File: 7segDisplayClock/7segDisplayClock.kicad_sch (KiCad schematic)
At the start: 26 parts, among them J1 USB_B_Micro, Q1 NPN, Q2 NPN, Q3 NPN, Q4 NPN, SW1 SW_Push, SW2 SW_Push, U1 HDSP-7503, U2 HDSP-7503, U3 HDSP-7503, U4 HDSP-7503, U5 PIC16F506, U6 74LS48

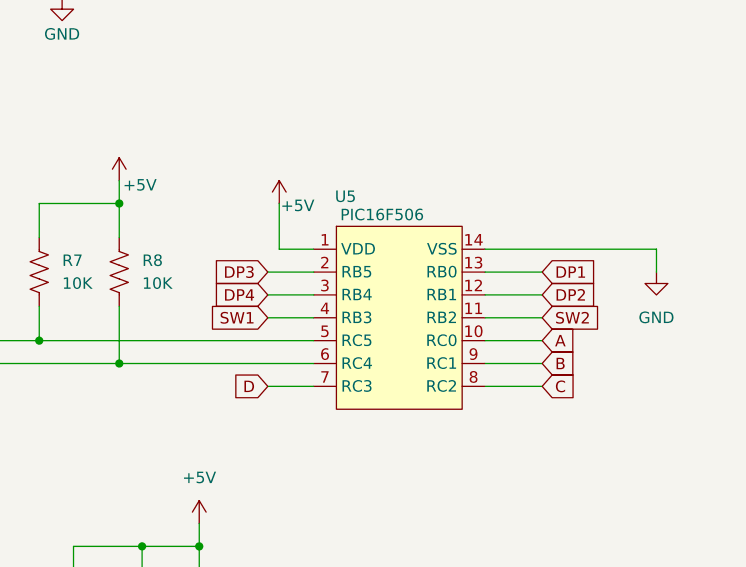
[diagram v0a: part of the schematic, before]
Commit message: BJT control signals change to match hardware
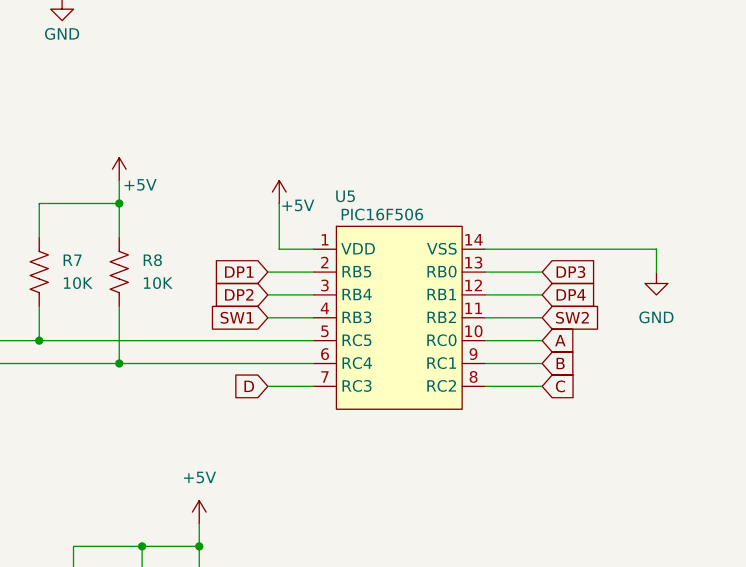
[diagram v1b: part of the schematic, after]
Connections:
- net DP1: now also U5.2 (RB5); no longer U5.13 (RB0)
- net DP2: now also U5.3 (RB4); no longer U5.12 (RB1)
- net DP3: now also U5.13 (RB0); no longer U5.2 (RB5)
- net DP4: now also U5.12 (RB1); no longer U5.3 (RB4)

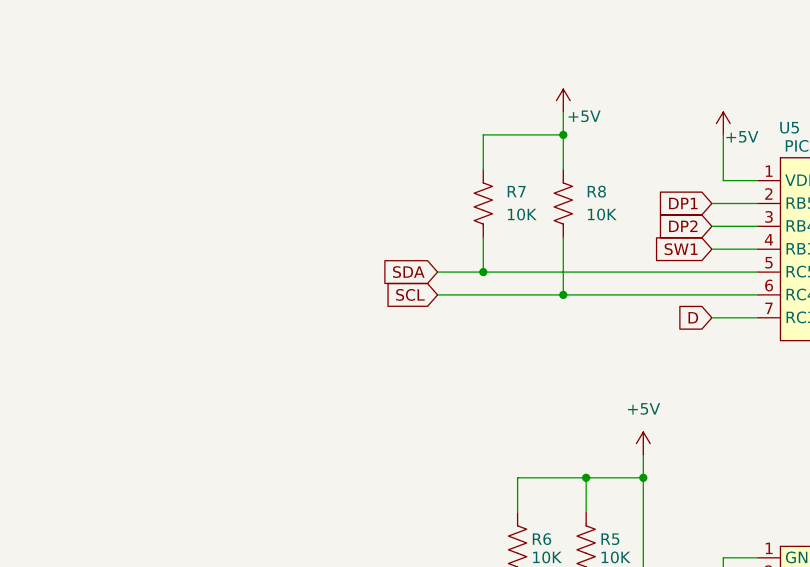
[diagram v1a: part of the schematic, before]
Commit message: SDA and SCL signals changed to match real hardware
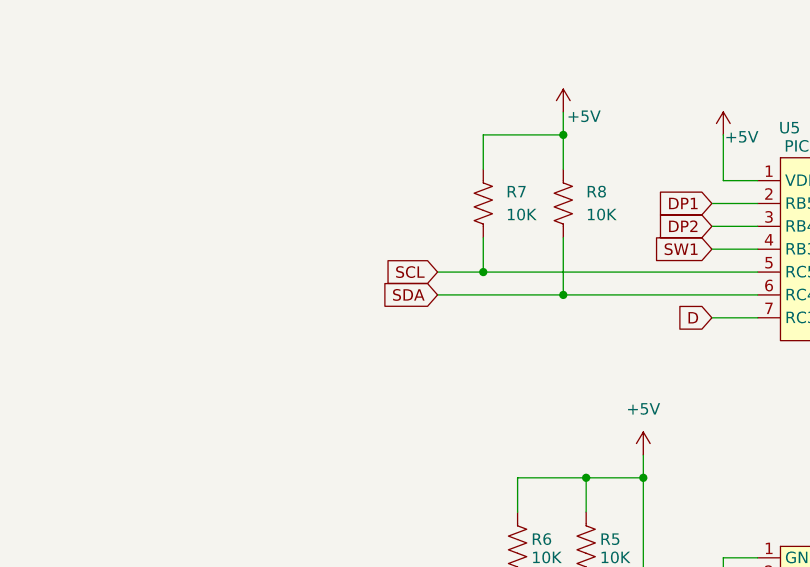
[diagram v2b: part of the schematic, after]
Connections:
- net SCL: now also R7.1, U5.5 (RC5); no longer R8.1, U5.6 (RC4)
- net SDA: now also R8.1, U5.6 (RC4); no longer R7.1, U5.5 (RC5)
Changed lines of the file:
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@@
+		)
+	)
+	(global_label "SDA"
+		(shape input)
+		(at 195.58 115.57 180)
+		(fields_autoplaced yes)
+		(effects
+			(font
+				(size 1.27 1.27)
+			)
+			(justify right)
+		)
+		(property "Intersheetrefs" "${INTERSHEET_REFS}"
+			(at 189.0267 115.57 0)
+			(effects
+				(font
+					(size 1.27 1.27)
+				)
+				(justify right)
+				(hide yes)
+			)
+		)
+	)
+	(global_label "DP4"
+		(shape input)
+		(at 256.54 107.95 0)
+		(fields_autoplaced yes)
+		(effects
+			(font
+				(size 1.27 1.27)
+			)
+			(justify left)
+		)
+		(property "Intersheetrefs" "${INTERSHEET_REFS}"
+			(at 263.2747 107.95 0)
+			(effects
+				(font
+					(size 1.27 1.27)
+				)
+				(justify left)
+				(hide yes)
+			)
+		)
+	)
+	(global_label "DP2"
+		(shape input)
+		(at 38.1 90.17 180)
+		(fields_autoplaced yes)
+		(effects
+			(font
+				(size 1.27 1.27)
+			)
+			(justify right)
+		)
+		(property "Intersheetrefs" "${INTERSHEET_REFS}"
+			(at 31.3653 90.17 0)
+			(effects
+				(font
+					(size 1.27 1.27)
+				)
+				(justify right)
+				(hide yes)
+			)
+		)
+	)
+	(global_label "DP1"
+		(shape input)
+		(at 38.1 53.34 180)
+		(fields_autoplaced yes)
+		(effects
+			(font
+				(size 1.27 1.27)
+			)
+			(justify right)
+		)
+		(property "Intersheetrefs" "${INTERSHEET_REFS}"
+			(at 31.3653 53.34 0)
+			(effects
+				(font
+					(size 1.27 1.27)
+				)
+				(justify right)
+				(hide yes)
+			)
+		)
+	)
+	(global_label "DP2"
+		(shape input)
+		(at 226.06 107.95 180)
+		(fields_autoplaced yes)
+		(effects
+			(font
+				(size 1.27 1.27)
+			)
+			(justify right)
+		)
+		(property "Intersheetrefs" "${INTERSHEET_REFS}"
+			(at 219.3253 107.95 0)
+			(effects
+				(font
+					(size 1.27 1.27)
+				)
+				(justify right)
+				(hide yes)
+			)
+		)
+	)
+	(global_label "C"
+		(shape input)
+		(at 140.97 99.06 0)
+		(fields_autoplaced yes)
+		(effects
+			(font
+				(size 1.27 1.27)
+			)
+			(justify left)
+		)
+		(property "Intersheetrefs" "${INTERSHEET_REFS}"
+			(at 145.2252 99.06 0)
+			(effects
+				(font
+					(size 1.27 1.27)
+				)
+				(justify left)
+				(hide yes)
+			)
+		)
+	)
+	(global_label "SW1"
+		(shape input)
+		(at 215.9 59.69 0)
+		(fields_autoplaced yes)
+		(effects
+			(font
+				(size 1.27 1.27)
+			)
+			(justify left)
+		)
+		(property "Intersheetrefs" "${INTERSHEET_REFS}"
+			(at 222.7556 59.69 0)
+			(effects
+				(font
+					(size 1.27 1.27)
+				)
+				(justify left)
+				(hide yes)
+			)
+		)
+	)
+	(global_label "SW2"
+		(shape input)
+		(at 256.54 110.49 0)
+		(fields_autoplaced yes)
+		(effects
+			(font
+				(size 1.27 1.27)
+			)
+			(justify left)
+		)
+		(property "Intersheetrefs" "${INTERSHEET_REFS}"
+			(at 263.3956 110.49 0)
+			(effects
+				(font
+					(size 1.27 1.27)
+				)
+				(justify left)
+				(hide yes)
+			)
+		)
+	)
+	(global_label "B"
+		(shape input)
+		(at 256.54 115.57 0)
+		(fields_autoplaced yes)
+		(effects
+			(font
+				(size 1.27 1.27)
+			)
+			(justify left)
+		)
+		(property "Intersheetrefs" "${INTERSHEET_REFS}"
+			(at 260.7952 115.57 0)
+			(effects
+				(font
+					(size 1.27 1.27)
+				)
+				(justify left)
+				(hide yes)
+			)
 		)
 	)
 	(global_label "SCL"
 		(shape input)
-		(at 195.58 115.57 180)
-		(fields_autoplaced yes)
-		(effects
-			(font
-				(size 1.27 1.27)
-			)
-			(justify right)
-		)
-		(property "Intersheetrefs" "${INTERSHEET_REFS}"
-			(at 189.0872 115.57 0)
-			(effects
-				(font
-					(size 1.27 1.27)
-				)
-				(justify right)
-				(hide yes)
-			)
-		)
-	)
-	(global_label "DP4"
-		(shape input)
-		(at 256.54 107.95 0)
-		(fields_autoplaced yes)
-		(effects
-			(font
-				(size 1.27 1.27)
-			)
-			(justify left)
-		)
-		(property "Intersheetrefs" "${INTERSHEET_REFS}"
-			(at 263.2747 107.95 0)
-			(effects
-				(font
-					(size 1.27 1.27)
-				)
-				(justify left)
-				(hide yes)
-			)
-		)
-	)
-	(global_label "DP2"
-		(shape input)
-		(at 38.1 90.17 180)
-		(fields_autoplaced yes)
-		(effects
-			(font
-				(size 1.27 1.27)
-			)
-			(justify right)
-		)
-		(property "Intersheetrefs" "${INTERSHEET_REFS}"
-			(at 31.3653 90.17 0)
-			(effects
-				(font
-					(size 1.27 1.27)
-				)
-				(justify right)
-				(hide yes)
-			)
-		)
-	)
-	(global_label "DP1"
-		(shape input)
-		(at 38.1 53.34 180)
-		(fields_autoplaced yes)
-		(effects
-			(font
-				(size 1.27 1.27)
-			)
-			(justify right)
-		)
-		(property "Intersheetrefs" "${INTERSHEET_REFS}"
-			(at 31.3653 53.34 0)
-			(effects
-				(font
-					(size 1.27 1.27)
-				)
-				(justify right)
-				(hide yes)
-			)
-		)
-	)
-	(global_label "DP2"
-		(shape input)
-		(at 226.06 107.95 180)
-		(fields_autoplaced yes)
-		(effects
-			(font
-				(size 1.27 1.27)
-			)
-			(justify right)
-		)
-		(property "Intersheetrefs" "${INTERSHEET_REFS}"
-			(at 219.3253 107.95 0)
-			(effects
-				(font
-					(size 1.27 1.27)
-				)
-				(justify right)
-				(hide yes)
-			)
-		)
-	)
-	(global_label "C"
-		(shape input)
-		(at 140.97 99.06 0)
-		(fields_autoplaced yes)
-		(effects
-			(font
-				(size 1.27 1.27)
-			)
-			(justify left)
-		)
-		(property "Intersheetrefs" "${INTERSHEET_REFS}"
-			(at 145.2252 99.06 0)
-			(effects
-				(font
-					(size 1.27 1.27)
-				)
-				(justify left)
-				(hide yes)
-			)
-		)
-	)
-	(global_label "SW1"
-		(shape input)
-		(at 215.9 59.69 0)
-		(fields_autoplaced yes)
-		(effects
-			(font
-				(size 1.27 1.27)
-			)
-			(justify left)
-		)
-		(property "Intersheetrefs" "${INTERSHEET_REFS}"
-			(at 222.7556 59.69 0)
-			(effects
-				(font
-					(size 1.27 1.27)
-				)
-				(justify left)
-				(hide yes)
-			)
-		)
-	)
-	(global_label "SW2"
-		(shape input)
-		(at 256.54 110.49 0)
-		(fields_autoplaced yes)
-		(effects
-			(font
-				(size 1.27 1.27)
-			)
-			(justify left)
-		)
-		(property "Intersheetrefs" "${INTERSHEET_REFS}"
-			(at 263.3956 110.49 0)
-			(effects
-				(font
-					(size 1.27 1.27)
-				)
-				(justify left)
-				(hide yes)
-			)
-		)
-	)
-	(global_label "B"
-		(shape input)
-		(at 256.54 115.57 0)
-		(fields_autoplaced yes)
-		(effects
-			(font
-				(size 1.27 1.27)
-			)
-			(justify left)
-		)
-		(property "Intersheetrefs" "${INTERSHEET_REFS}"
-			(at 260.7952 115.57 0)
-			(effects
-				(font
-					(size 1.27 1.27)
-				)
-				(justify left)
-				(hide yes)
-			)
-		)
-	)
-	(global_label "SDA"
-		(shape input)
 		(at 195.58 113.03 180)
 		(fields_autoplaced yes)
@@
 		)
 		(property "Intersheetrefs" "${INTERSHEET_REFS}"
-			(at 189.0267 113.03 0)
-			(effects
-				(font
+			(at 189.0872 113.03 0)
+			(effects
+				(font
